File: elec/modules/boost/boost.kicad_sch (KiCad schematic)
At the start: 9 parts, among them J1 Conn_01x05, J2 Conn_01x05, U1 LM2587S-ADJ

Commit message: sleepy but did most pcbs
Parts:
- removed J1, J2: Conn_01x05, Pinheaders:PinHeader_1x05_P2.54mm_Vertical, symbol Connector_Generic:Conn_01x05
- added C35: 0.1uF, Capacitor_SMD:C_0603_1608Metric, symbol Device:C
- added C36: 100uF, Capacitor_THT:CP_Radial_D8.0mm_P3.50mm, symbol Device:C_Polarized
- added J1, J2: Conn_01x08, Pinheaders:PinHeader_1x08_P2.54mm_Vertical, symbol Connector_Generic:Conn_01x08
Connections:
- net +12V: now also C35.1, C36.1, J1.1 (Pin_1), J1.2 (Pin_2), J1.3 (Pin_3)
- net +24V: now also J2.3 (Pin_3), J2.4 (Pin_4), J2.5 (Pin_5), J2.6 (Pin_6)
- net GND: now also C35.2, C36.2, J1.6 (Pin_6), J1.7 (Pin_7), J1.8 (Pin_8)
- no-connect marks 0 -> 6

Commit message: added Bourns TC33X-2-104E
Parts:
- removed R35: 36.9K/56k, Capacitor_SMD:C_0603_1608Metric, symbol Device:R
- added VR1: TC33X-2-104E, Bourns TC33X-2-104E:TC33X2104E, symbol TC33X-2-104E:TC33X-2-104E
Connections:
- net +24V: now also VR1.3 (CW)
- net at R36.1, U1.2 (FB): now also VR1.1 (CCW), VR1.2 (WIPER)
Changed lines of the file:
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@@
+	)
+	(junction
+		(at 163.83 80.01)
+		(diameter 0)
+		(color 0 0 0 0)
 	)
 	(junction
@@
 	)
 	(junction
+		(at 198.12 71.12)
+		(diameter 0)
+		(color 0 0 0 0)
+	)
+	(junction
 		(at 127 111.76)
 		(diameter 0)
@@
 	)
 	(junction
-		(at 163.83 71.12)
-		(diameter 0)
-		(color 0 0 0 0)
-	)
-	(junction
 		(at 163.83 85.09)
 		(diameter 0)
@@
 	(wire
 		(pts
+			(xy 198.12 77.47) (xy 198.12 71.12)
+		)
+		(stroke
+			(width 0)
+			(type default)
+		)
+	)
+	(wire
+		(pts
 			(xy 101.6 111.76) (xy 124.46 111.76)
 		)
@@
 	(wire
 		(pts
-			(xy 163.83 71.12) (xy 163.83 74.93)
-		)
-		(stroke
-			(width 0)
-			(type default)
-		)
-	)
-	(wire
-		(pts
 			(xy 146.05 71.12) (xy 129.54 71.12)
 		)
@@
 	(wire
 		(pts
+			(xy 198.12 71.12) (xy 220.98 71.12)
+		)
+		(stroke
+			(width 0)
+			(type default)
+		)
+	)
+	(wire
+		(pts
+			(xy 194.31 77.47) (xy 198.12 77.47)
+		)
+		(stroke
+			(width 0)
+			(type default)
+		)
+	)
+	(wire
+		(pts
 			(xy 144.78 82.55) (xy 146.05 82.55)
 		)
@@
 	(wire
 		(pts
-			(xy 163.83 71.12) (xy 158.75 71.12)
+			(xy 158.75 71.12) (xy 198.12 71.12)
 		)
 		(stroke
@@
 	(wire
 		(pts
-			(xy 163.83 82.55) (xy 163.83 85.09)
-		)
-		(stroke
-			(width 0)
-			(type default)
-		)
-	)
-	(wire
-		(pts
 			(xy 77.47 71.12) (xy 91.44 71.12)
 		)
@@
 	(wire
 		(pts
-			(xy 163.83 71.12) (xy 220.98 71.12)
-		)
-		(stroke
-			(width 0)
-			(type default)
-		)
-	)
-	(wire
-		(pts
 			(xy 91.44 71.12) (xy 101.6 71.12)
 		)
@@
 	(wire
 		(pts
+			(xy 163.83 80.01) (xy 163.83 85.09)
+		)
+		(stroke
+			(width 0)
+			(type default)
+		)
+	)
+	(wire
+		(pts
 			(xy 58.42 92.71) (xy 62.23 92.71)
 		)
@@
 		(pts
 			(xy 45.72 90.17) (xy 45.72 92.71)
+		)
+		(stroke
+			(width 0)
+			(type default)
+		)
+	)
+	(wire
+		(pts
+			(xy 163.83 74.93) (xy 163.83 80.01)
 		)
 		(stroke
@@
 	)
 	(symbol
-		(lib_id "Device:R")
-		(at 163.83 78.74 0)
-		(mirror y)
-		(unit 1)
-		(exclude_from_sim no)
-		(in_bom yes)
-		(on_board yes)
-		(dnp no)
-		(property "Reference" "R35"
-			(at 162.052 78.105 0)
-			(effects
-				(font
-					(size 1.27 1.27)
-				)
-				(justify left)
-			)
-		)
-		(property "Value" "36.9K/56k"
-			(at 162.052 80.264 0)
-			(effects
-				(font
-					(size 1.27 1.27)
-				)
-				(justify left)
-			)
-		)
-		(property "Footprint" "Capacitor_SMD:C_0603_1608Metric"
-			(at 165.608 78.74 90)
-			(effects
-				(font
-					(size 1.27 1.27)
-				)
-				(hide yes)
-			)
-		)
-		(property "Datasheet" "~"
-			(at 163.83 78.74 0)
-			(effects
-				(font
-					(size 1.27 1.27)
-				)
-				(hide yes)
-			)
-		)
-		(property "Description" ""
-			(at 163.83 78.74 0)
-			(effects
-				(font
-					(size 1.27 1.27)
-				)
-				(hide yes)
-			)
-		)
-		(property "LCSC" "C23082"
-			(at 163.83 78.74 0)
-			(effects
-				(font
-					(size 1.27 1.27)
-				)
-				(hide yes)
-			)
-		)
-		(pin "1"
-		)
-		(pin "2"
-		)
-		(instances
-			(project "boost"
-				(path "/97baff51-d1b5-4933-bf19-f5d3c53b231d"
-					(reference "R35")
-					(unit 1)
-				)
-			)
-		)
-	)
-	(symbol
 		(lib_id "power:GND")
 		(at 60.96 90.17 90)
@@
 					(unit 1)
 				)
+			)
+		)
+	)
+	(symbol
+		(lib_id "TC33X-2-104E:TC33X-2-104E")
+		(at 194.31 74.93 270)
+		(unit 1)
+		(exclude_from_sim no)
+		(in_bom yes)
+		(on_board yes)
+		(dnp no)
+		(fields_autoplaced yes)
+		(property "Reference" "VR1"
+			(at 179.07 67.31 90)
+			(effects
+				(font
+					(size 1.27 1.27)
+				)
+			)
+		)
+		(property "Value" "TC33X-2-104E"
+			(at 179.07 69.85 90)
+			(effects
+				(font
+					(size 1.27 1.27)
+				)
+			)
+		)
+		(property "Footprint" "Bourns TC33X-2-104E:TC33X2104E"
+			(at 91.77 83.82 0)
+			(effects
+				(font
+					(size 1.27 1.27)
+				)
+				(justify left top)
+				(hide yes)
+			)
+		)
+		(property "Datasheet" "https://www.bourns.com/docs/Product-Datasheets/TC33.pdf"
+			(at -8.23 83.82 0)
+			(effects
+				(font
+					(size 1.27 1.27)
+				)
+				(justify left top)
+				(hide yes)
+			)
+		)
+		(property "Description" "Trimmer Resistors - SMD 3MM 100KOHMS 25% 0.1WATT OPEN FRM"
+			(at 194.31 74.93 0)
+			(effects
+				(font
+					(size 1.27 1.27)
+				)
+				(hide yes)
+			)
+		)
+		(property "Height" "1.5"
+			(at -208.23 83.82 0)
+			(effects
+				(font
+					(size 1.27 1.27)
+				)
+				(justify left top)
+				(hide yes)
+			)
+		)
+		(property "Mouser Part Number" "652-TC33X-2-104E"
+			(at -308.23 83.82 0)
+			(effects
+				(font
+					(size 1.27 1.27)
+				)
+				(justify left top)
+				(hide yes)
+			)
+		)
+		(property "Mouser Price/Stock" "https://www.mouser.co.uk/ProductDetail/Bourns/TC33X-2-104E?qs=2hAPiALdQ0llyX8B3WfcDg%3D%3D"
+			(at -408.23 83.82 0)
+			(effects
+				(font
+					(size 1.27 1.27)
+				)
+				(justify left top)
+				(hide yes)
+			)
+		)
+		(property "Manufacturer_Name" "Bourns"
+			(at -508.23 83.82 0)
+			(effects
+				(font
+					(size 1.27 1.27)
+				)
+				(justify left top)
+				(hide yes)
+			)
+		)
+		(property "Manufacturer_Part_Number" "TC33X-2-104E"
+			(at -608.23 83.82 0)
+			(effects
+				(font
+					(size 1.27 1.27)
+				)
+				(justify left top)
+				(hide yes)
+			)
+		)
+		(pin "2"
+		)
+		(pin "3"
+		)
+		(pin "1"
+		)
+		(instances
+			(project ""
+				(path "/97baff51-d1b5-4933-bf19-f5d3c53b231d"
+					(reference "VR1")
+					(unit 1)
+				)

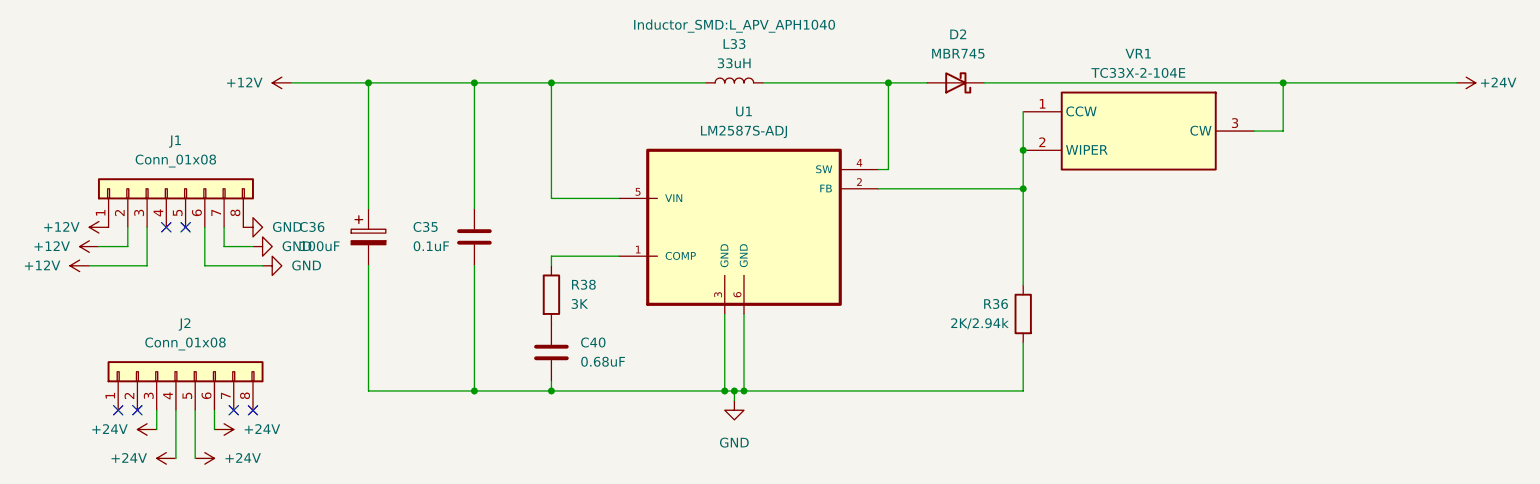
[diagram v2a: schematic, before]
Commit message: feat: added pot to boost
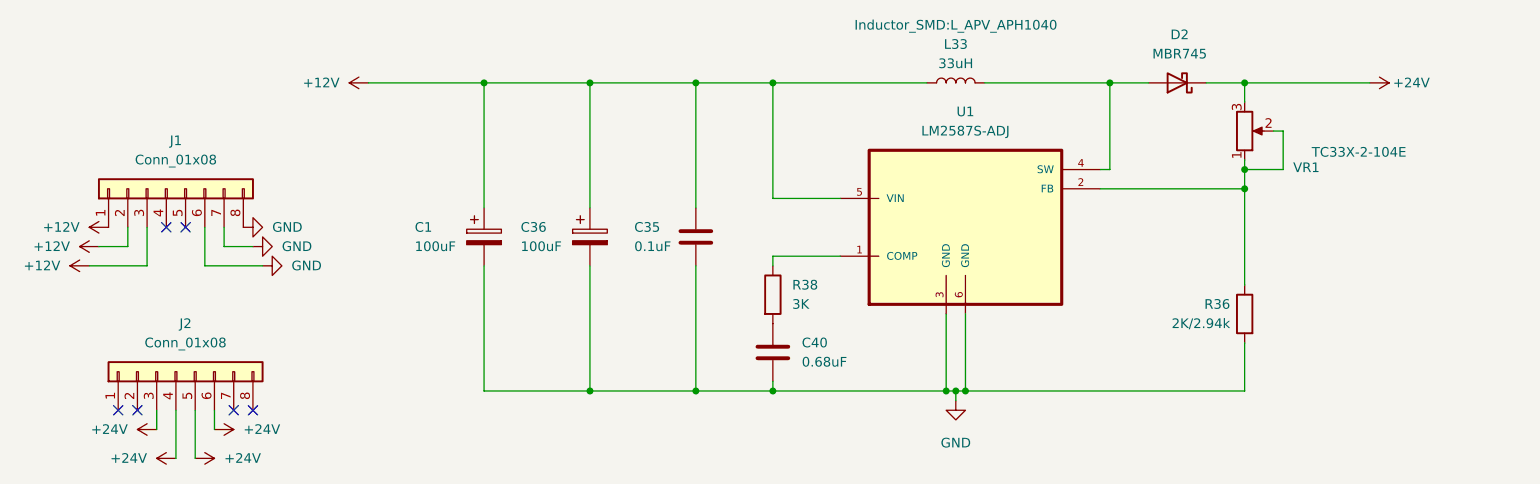
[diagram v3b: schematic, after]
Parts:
- added C1: 100uF, Capacitor_THT:CP_Radial_D8.0mm_P3.50mm, symbol Device:C_Polarized
- VR1: symbol TC33X-2-104E:TC33X-2-104E -> Device:R_Potentiometer
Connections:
- net +12V: now also C1.1
- net GND: now also C1.2
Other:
- moved on the sheet: C35, C36, C40, D2, L33, R36, R38, U1
